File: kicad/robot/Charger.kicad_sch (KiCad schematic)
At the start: 32 parts, among them U13 MAX77976EFD+

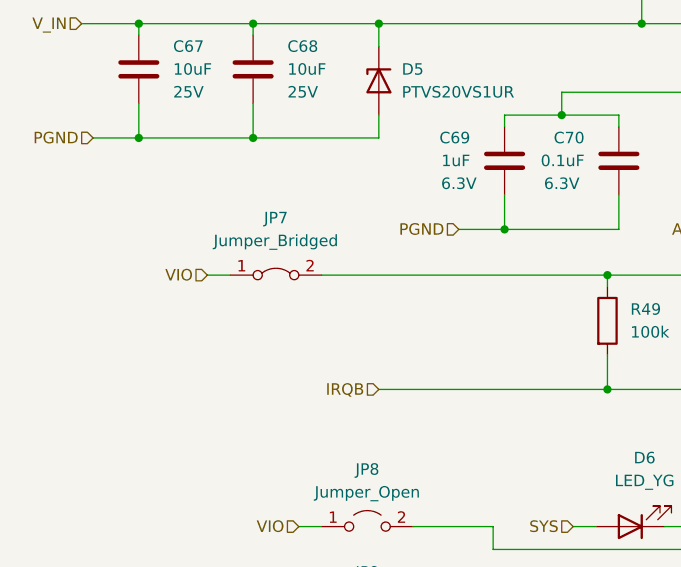
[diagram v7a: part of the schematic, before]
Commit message: Added separate jumpers
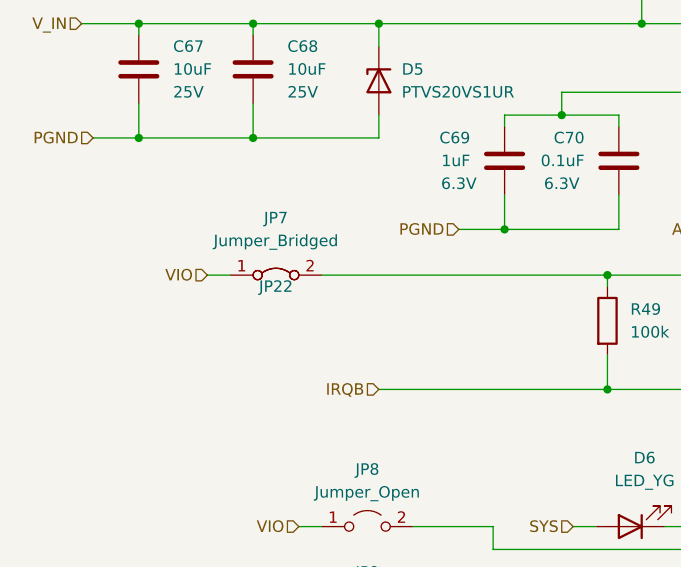
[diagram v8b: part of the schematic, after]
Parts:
- added JP22: Jumper, custom_connectors:2.54mm_2pointJumper, symbol Jumper:Jumper
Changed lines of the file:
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@@
     (pin "2")
+  )
+  (symbol (lib_id "Jumper:Jumper") (at 33.02 109.22 0) (unit 1)
+    (in_bom yes) (on_board yes)
+    (property "Reference" "JP22" (id 0) (at 33.02 110.49 0))
+    (property "Value" "Jumper" (id 1) (at 33.02 111.76 0)
+      (effects (font (size 1.27 1.27)) hide)
+    )
+    (property "Footprint" "custom_connectors:2.54mm_2pointJumper" (id 2) (at 33.02 117.475 0)
+      (effects (font (size 1.27 1.27)) hide)
+    )
+    (property "Datasheet" "~" (id 3) (at 33.02 109.22 0)
+      (effects (font (size 1.27 1.27)) hide)
+    )
   )
   (symbol (lib_id "Device:C") (at 205.74 102.87 0) (mirror y) (unit 1)
